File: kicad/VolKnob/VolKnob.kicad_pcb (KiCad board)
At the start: 2 copper layers, 40.6 x 40.6 mm, 3 parts, among them P1 CONNECTOR, SW1 Rotary_Encoder

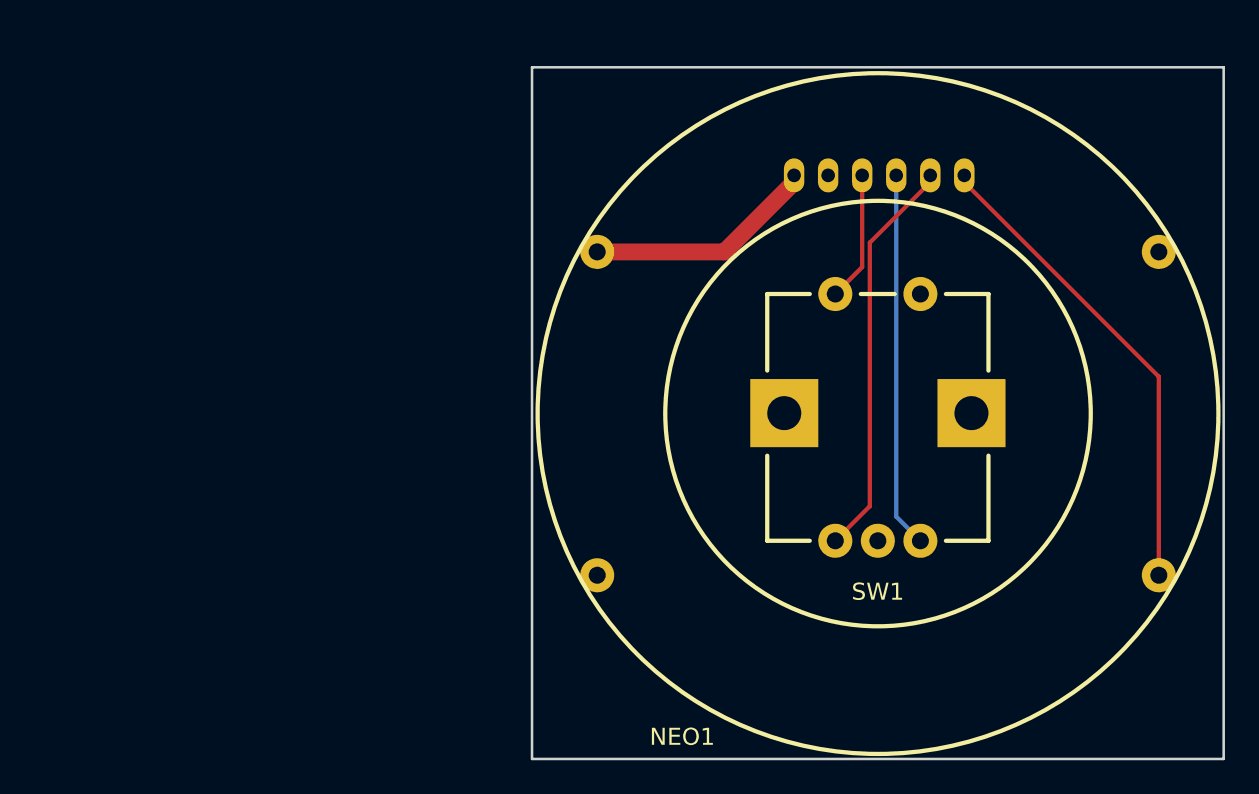
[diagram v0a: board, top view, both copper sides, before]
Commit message: Modified circuit to allow for hardware debounce
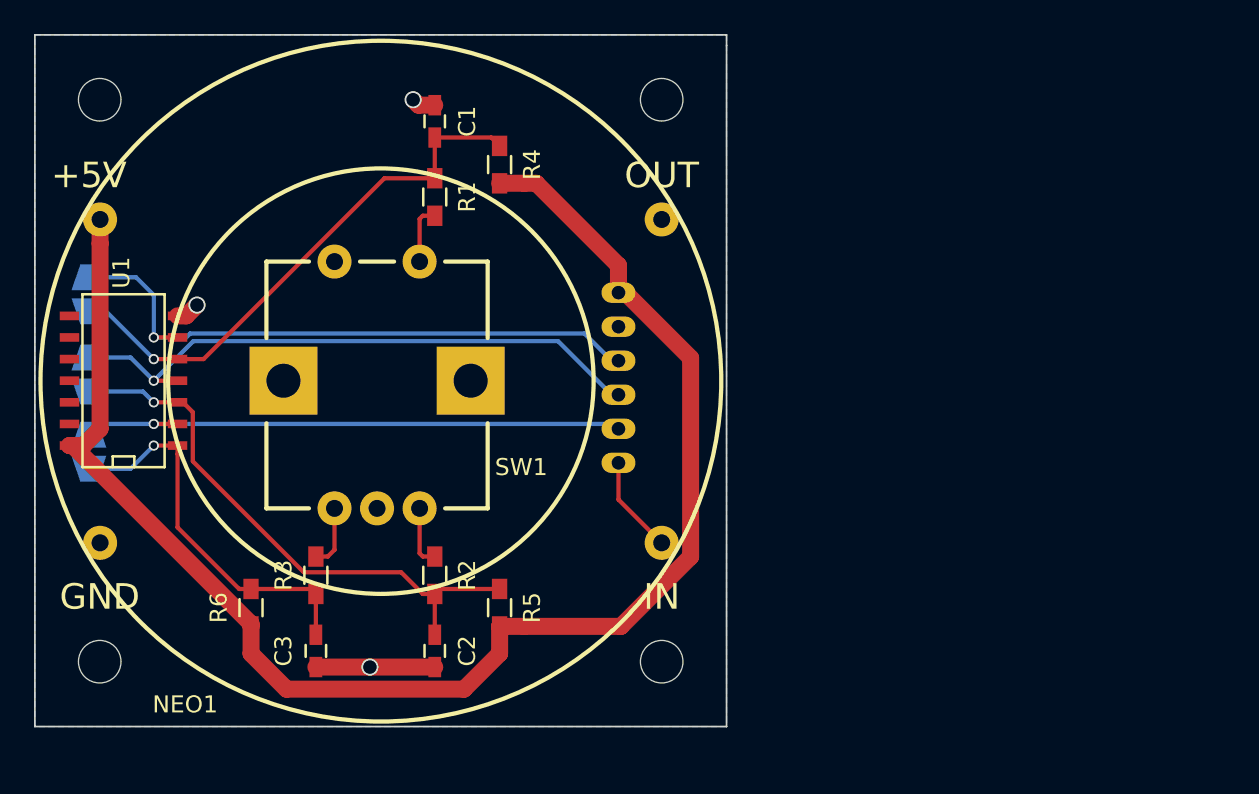
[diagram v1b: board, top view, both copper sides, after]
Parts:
- added C1: 100n, Capacitors_SMD:C_0603_HandSoldering, F.Cu at (122.6, 88.3)
- added C2: 100n, Capacitors_SMD:C_0603_HandSoldering, F.Cu at (122.6, 119.4)
- added C3: 100n, Capacitors_SMD:C_0603_HandSoldering, F.Cu at (115.6, 119.4)
- added JP1: Jumper_NO_Small, jumpers:Jumper_NO, B.Cu at (102.2, 98.4)
- added JP2: Jumper_NO_Small, jumpers:Jumper_NO, B.Cu at (102.2, 103.1)
- added JP3: Jumper_NO_Small, jumpers:Jumper_NO, B.Cu at (102.2, 107.7)
- added R1: 2k2, Resistors_SMD:R_0603_HandSoldering, F.Cu at (122.6, 92.7)
- added R2: 2k2, Resistors_SMD:R_0603_HandSoldering, F.Cu at (122.6, 114.9)
- added R3: 2k2, Resistors_SMD:R_0603_HandSoldering, F.Cu at (115.6, 114.9)
- added R4: 10k, Resistors_SMD:R_0603_HandSoldering, F.Cu at (126.4, 90.8)
- added R5: 10k, Resistors_SMD:R_0603_HandSoldering, F.Cu at (126.4, 116.8)
- added R6: 10k, Resistors_SMD:R_0603_HandSoldering, F.Cu at (111.8, 116.8)
- added REF**: MountingHole_2.5mm, Mounting_Holes:MountingHole_2.5mm, F.Cu at (135.9, 87.0)
- added REF**: MountingHole_2.5mm, Mounting_Holes:MountingHole_2.5mm, F.Cu at (102.9, 87.0)
- added REF**: MountingHole_2.5mm, Mounting_Holes:MountingHole_2.5mm, F.Cu at (102.9, 120.0)
- added REF**: MountingHole_2.5mm, Mounting_Holes:MountingHole_2.5mm, F.Cu at (135.9, 120.0)
- added U1: 74HC14, SMD_Packages:SOIC-14_N, F.Cu at (104.1, 103.5)
- moved SW1 29.5 mm to (119.2, 103.5)
- moved NEO1 29.3 mm to (119.4, 103.5)
- moved P1 19.4 mm to (133.3, 103.3), turned to 270 degrees
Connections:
- net /+5V renamed +5V
- NEO1 pad 2: /Gnd -> GND
- P1 pad 2: /Gnd -> GND
- SW1 pad 1: /Gnd -> Net-(R1-Pad2)
- SW1 pad 2: /Btn -> GND
- SW1 pad 3: /ROT_A -> Net-(R2-Pad2)
- SW1 pad 4: /Gnd -> GND
- SW1 pad 5: /ROT_B -> Net-(R3-Pad2)
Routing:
- net +5V: track 13.7 -> 90.2 mm
- net Net-(C2-Pad1): track 0.00 -> 33.3 mm, vias 0 -> 1
- net Net-(C1-Pad1): track 0.00 -> 32.3 mm, vias 0 -> 1
- net /Btn: track 7.62 -> 36.2 mm, vias 0 -> 1
- net Net-(C3-Pad1): track 0.00 -> 22.7 mm, vias 0 -> 1
- net /NEO: track 28.2 -> 5.75 mm
- net /ROT_A: track 22.1 -> 35.3 mm, vias 0 -> 1
- net GND: track 0.00 -> 9.79 mm, vias 0 -> 3
- net /ROT_B: track 23.8 -> 32.9 mm, vias 0 -> 1
- net Net-(R3-Pad2): track 0.00 -> 3.69 mm
- net Net-(R2-Pad2): track 0.00 -> 3.61 mm
- net Net-(R1-Pad2): track 0.00 -> 3.47 mm
- added copper zone on B.Cu, net GND
- removed copper zone on B.Cu, net /Gnd
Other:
- outline, holes or cut-outs redrawn
- rule pad_to_mask_clearance: 0.2 -> 0
- board text added: "+5V"
- board text added: "GND"
- board text added: "IN"
- board text added: "OUT"
- board text added: "v@nce.me Neopixel Input V1.0"
- board text removed: "v@nce.me Rotary Input V1.0"

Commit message: Minor updates and board submitted for fabrication
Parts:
- removed the REF** at (135.9, 87.0)
- removed the REF** at (102.9, 87.0)
- removed the REF** at (102.9, 120.0)
- removed the REF** at (135.9, 120.0)
- added D1: LED, SMD_LED:LED_SMD_1.6x0.8mm, B.Cu at (108.6, 88.3)
- added D2: LED, SMD_LED:LED_SMD_1.6x0.8mm, B.Cu at (125.1, 88.3)
- added D3: LED, SMD_LED:LED_SMD_1.6x0.8mm, B.Cu at (130.2, 88.3)
- added R7: 220, Resistors_SMD:R_0603_HandSoldering, B.Cu at (108.6, 90.8)
- added R8: 220, Resistors_SMD:R_0603_HandSoldering, B.Cu at (125.1, 90.8)
- added R9: 220, Resistors_SMD:R_0603_HandSoldering, B.Cu at (130.3, 90.8)
- added REF**: MountingHole_2.7mm_M2.5_ISO7380_Pad, Mounting_Holes:MountingHole_2.7mm_M2.5_ISO7380_Pad, F.Cu at (102.9, 87.0)
- added REF**: MountingHole_2.7mm_M2.5_ISO7380_Pad, Mounting_Holes:MountingHole_2.7mm_M2.5_ISO7380_Pad, F.Cu at (102.9, 120.0)
- added REF**: MountingHole_2.7mm_M2.5_ISO7380_Pad, Mounting_Holes:MountingHole_2.7mm_M2.5_ISO7380_Pad, F.Cu at (135.9, 120.0)
- added REF**: MountingHole_2.7mm_M2.5_ISO7380_Pad, Mounting_Holes:MountingHole_2.7mm_M2.5_ISO7380_Pad, F.Cu at (135.9, 87.0)
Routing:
- net /ROT_A: track 35.3 -> 62.2 mm
- net /ROT_B: track 32.9 -> 59.3 mm
- net /Btn: track 36.2 -> 47.7 mm
- net Net-(D2-Pad1): track 0.00 -> 2.62 mm
- net Net-(D1-Pad1): track 0.00 -> 2.62 mm
- net Net-(D3-Pad1): track 0.00 -> 2.55 mm
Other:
- board text added: "A"
- board text added: "B"
- board text added: "BTN"
